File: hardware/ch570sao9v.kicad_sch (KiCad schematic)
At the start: 45 parts, among them J1 SAO, SW1 TS-1187A-B-A-B, SW2 TS-1187A-B-A-B, SW3 TS-1187A-B-A-B, SW4 SW_SPDT, U2 TPS54302, U3 CH572Q, U4 HX3608_BOOST, Y1 32MHz

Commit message: Update design
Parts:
- added C16: 1u, Resistor_SMD:R_0402_1005Metric, symbol Device:C
- added C17, C18: 100n, Resistor_SMD:R_0402_1005Metric, symbol Device:C
- added R4: 33, cnhardware:R_0402_1005Metric_COMPACT, symbol Device:R
- added R9: 33k, cnhardware:R_0402_1005Metric_COMPACT, symbol Device:R
- added U5: ~, cnhardware:LGA-14_3x2.5mm_P0.5mm_LayoutBorder3x4y_EVEN_PADS, symbol cnhardware:LSM6DSL
- added U6: QMC6309, Package_BGA:WLP-4_0.83x0.83mm_P0.4mm, symbol cnhardware:QMC6309
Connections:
- net BS1: now also U5.13 (SCL), U6.A2 (SCL)
- net D/C: now also R9.1, U5.14 (SDA), U6.B2 (SDA)
- net GND: now also C16.2, C17.2, C18.2, U5.1 (SA0), U5.2 (SDx), U5.3 (SCx), U5.6 (GND), U5.7 (GND), U6.A1 (VSS)
- net VDD: now also C18.1, R4.1, R9.2, U5.12 (CS), U5.5 (VDDIO)
- new net IMUVC: C16.1, C17.1, R4.2, U5.8 (VDD), U6.B1 (VDD)
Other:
- note added: "REV A UNTESTED"

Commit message: Update to rev a
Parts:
- added D2: 1N4148, Diode_SMD:D_SOD-323, symbol Diode:1N4148
- BT1, SW1, SW2, SW3, U1: now not fitted; now left out of the parts list
- SW4: LCSC C963206 -> C3008585
- TP1: value MOSITP -> MOSI; now not fitted
- TP2, TP7, TP8, TP9: now not fitted
- TP3: value DCTP -> SCK; now not fitted
- TP4: value DCTP -> DC; now not fitted
- TP5: value SCSTP -> SCS; now not fitted
- TP6: value RESTP -> RES; now not fitted
- U5: value ~ -> LSM6DS3
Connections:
- net +9V: now also D2.1 (K); no longer SW4.2 (B)
- new net: D2.2 (A), SW4.2 (B)
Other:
- moved on the sheet: C1, C13, C14, C2, C6, R6, SW4, U3, Y1

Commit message: Update rev a
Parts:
- added C19: 4.7u, Capacitor_SMD:C_1206_3216Metric, symbol Device:C
- R4: value 33 -> 10; LCSC C25105 -> C25077
- U5: LCSC C967633 -> C784817
- Y1: LCSC C7294697 -> C37635323
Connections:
- net GND: now also C19.1
- net IMUVC: now also C19.2
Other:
- note added: "IMU can be: C967633 - LSM6DS3 C784817 - LSM6DSR"
- moved on the sheet: C16, C17, C18, R4

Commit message: Bump design
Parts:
- TP7, TP9: LCSC (none) -> C6063943
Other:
- note added: "Battery Terminals: MUST BE Keystone 1016-1 (36-1016-1-ND) D2 is not actually needed IRL, but just in case"
- note added: "CHANGES: RevA->B * Fixed back label"
- note added: "REV A UNTESTED TODO: Antenna tuning test. Bring OLED pads down about 0.2mm, same size.. Fix labeling on back"
- note removed: "REV A UNTESTED"
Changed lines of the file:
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@@
 	(generator_version "9.0")
 	(paper "A4")
-	(text "REV A UNTESTED"
+	(text "REV A UNTESTED\nTODO: Antenna tuning test.\nBring OLED pads down about 0.2mm, same size..\nFix labeling on back"
 		(exclude_from_sim no)
-		(at 53.848 110.236 0)
+		(at 157.226 28.448 0)
 		(effects
 			(font
@@
 		)
 	)
+	(text "CHANGES:\n\nRevA->B\n * Fixed back label\n"
+		(exclude_from_sim no)
+		(at 45.974 118.364 0)
+		(effects
+			(font
+				(size 1.27 1.27)
+			)
+		)
+	)
+	(text "Battery Terminals:\nMUST BE Keystone 1016-1 (36-1016-1-ND)\nD2 is not actually needed IRL, but just in case"
+		(exclude_from_sim no)
+		(at 147.066 106.68 0)
+		(effects
+			(font
+				(size 1.27 1.27)
+			)
+		)
+	)
 	(text "BS1: 1: I2C / 0: SPI\nRONBOE\nRB150-2828KSWKG01"
 		(exclude_from_sim no)
@@
 			)
 		)
+		(property "LCSC" "C6063943"
+			(at 105.41 142.24 90)
+			(effects
+				(font
+					(size 1.27 1.27)
+				)
+				(hide yes)
+			)
+		)
 		(pin "1"
 		)
@@
 			(effects
 				(font
+					(size 1.27 1.27)
+				)
+				(hide yes)
+			)
+		)
+		(property "LCSC" "C6063943"
+			(at 105.41 137.16 90)
+			(effects
+				(font

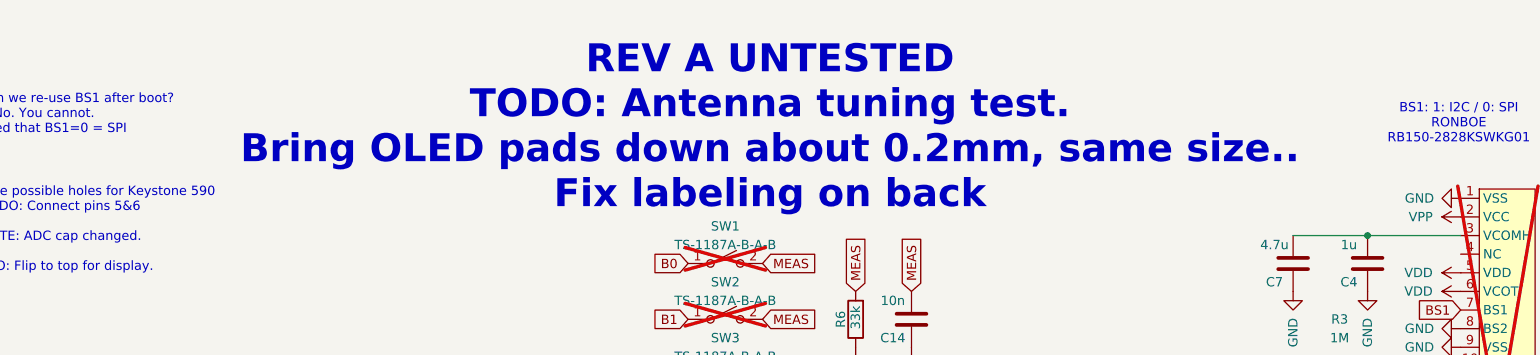
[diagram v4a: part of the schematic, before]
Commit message: Remove firmware.experiment, and update design
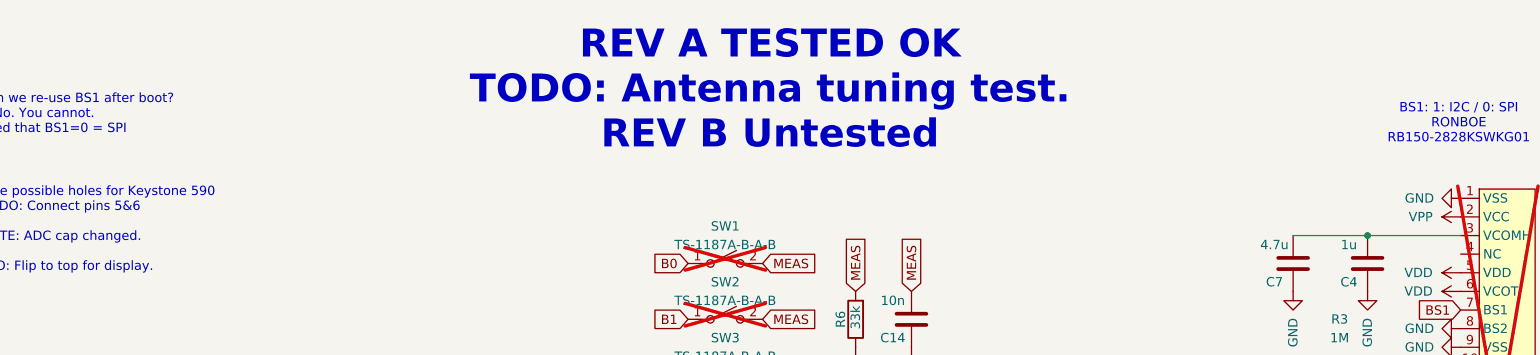
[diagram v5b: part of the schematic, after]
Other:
- note added: "REV A TESTED OK TODO: Antenna tuning test. REV B Untested"
- note removed: "REV A UNTESTED TODO: Antenna tuning test. Bring OLED pads down about 0.2mm, same size.. Fix labeling on back"
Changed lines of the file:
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@@
 	(generator_version "9.0")
 	(paper "A4")
-	(text "REV A UNTESTED\nTODO: Antenna tuning test.\nBring OLED pads down about 0.2mm, same size..\nFix labeling on back"
+	(text "REV A TESTED OK\nTODO: Antenna tuning test.\nREV B Untested"
 		(exclude_from_sim no)
-		(at 157.226 28.448 0)
+		(at 157.226 23.368 0)
 		(effects
 			(font
